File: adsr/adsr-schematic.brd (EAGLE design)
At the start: 160 x 100 mm, 28 parts, among them IC1 NE555N, IC2 LM358N, Q1 BC548B, Q2 BC548B, Q3 BC548B

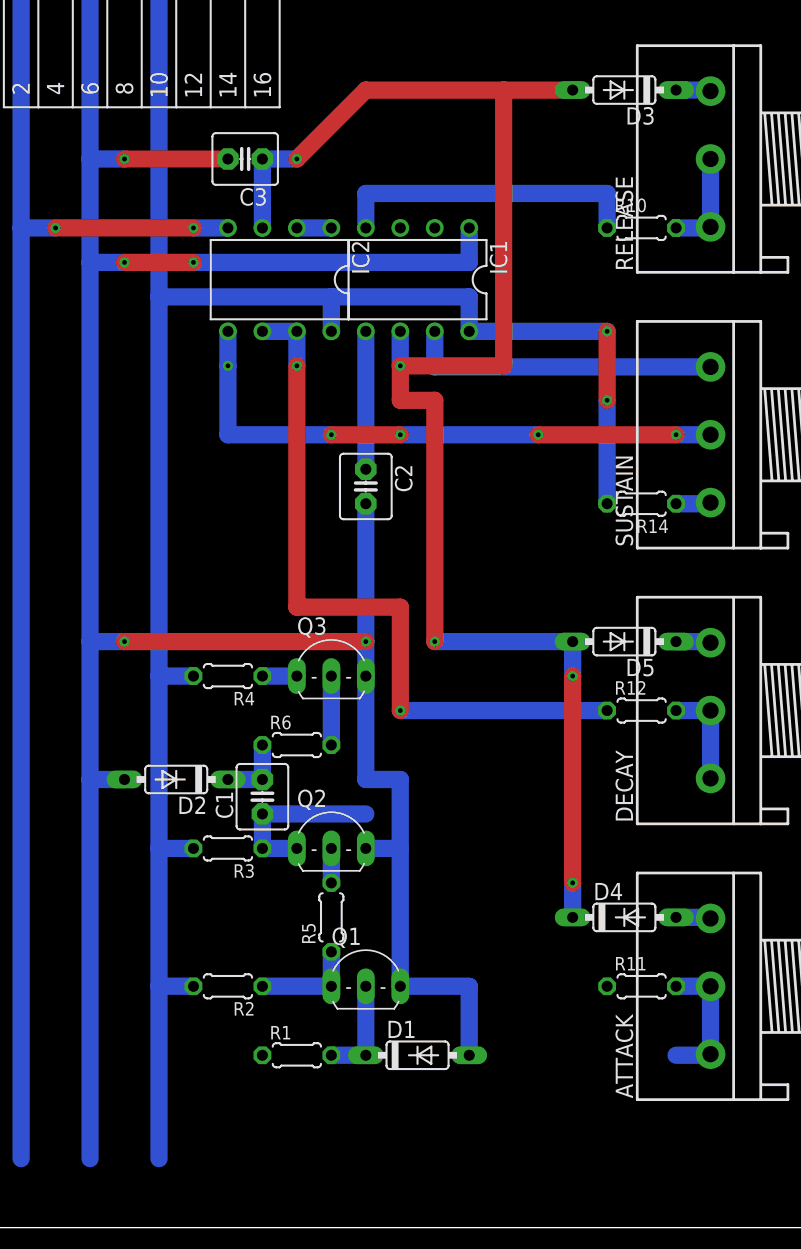
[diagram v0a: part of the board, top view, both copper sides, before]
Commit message: save sequencer and adsr.
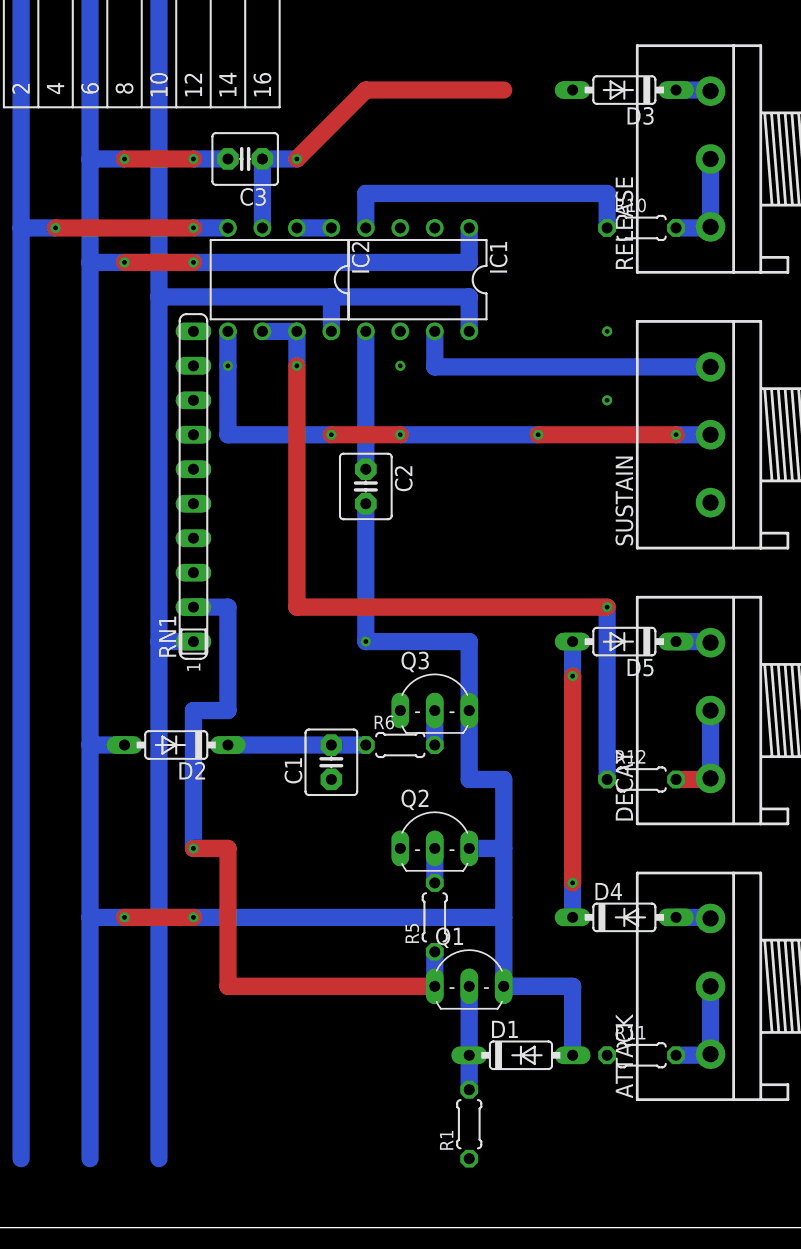
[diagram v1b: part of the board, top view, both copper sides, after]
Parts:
- removed R14, R2, R3, R4: 4.7k, rcl:0204/5
- added RN1: 4.7k, resistor-sil:SIL10
- moved R1 13.7 mm to (35.6, 7.62), turned to 90 degrees
- moved Q3 8.03 mm to (33.0, 39.4)
- moved Q2 7.62 mm to (33.0, 29.2)
- moved R5 7.62 mm to (33.0, 22.9)
- moved Q1 7.62 mm to (35.6, 19.1)
- moved R6 7.62 mm to (30.5, 35.6)
- moved D1 7.62 mm to (39.4, 12.7)
- moved C1 5.68 mm to (25.4, 34.3)
- moved R11 5.08 mm to (48.3, 12.7)
- moved R12 5.08 mm to (48.3, 33.0)
- moved D2 2.54 mm to (14.0, 35.6)
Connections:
- net +12V: now also RN1.1; no longer R14.2, R2.2, R3.2, R4.2
- net N$17: now also RN1.5; no longer R14.1
- net N$2: now also RN1.2; no longer R2.1
- net N$3: now also RN1.3; no longer R3.1
- net N$4: now also RN1.4; no longer R4.1
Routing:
- net N$12: track 113.9 -> 45.3 mm, vias 5 -> 4
- net N$2: track 7.62 -> 53.3 mm, vias 0 -> 1
- net +12V: track 147.3 -> 119.4 mm
- net GND: track 213.4 -> 231.1 mm, vias 6 -> 7
- net N$3: track 35.6 -> 22.9 mm
- net N$7: track 5.08 -> 10.2 mm
- net N$18: track 53.3 -> 58.4 mm
- net N$9: track 10.2 -> 7.62 mm
- net N$17: track 2.62 -> 0.08 mm
- net N$6: track 5.08 -> 2.54 mm
- net N$4: track 2.54 -> 0.00 mm
